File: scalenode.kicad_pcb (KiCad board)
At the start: 4 copper layers, 135.5 x 40 mm, 137 parts, among them IC1 TPS2378DDA, J1 B2B-XH-A_LF__SN_, J10 LSHM-130-01-L-RH-A-S-K-TR, J3 1-2199230-6, J4 1140084168, J5 0473460001, J6 SS-74800-144, J7 DF40HC(3.0)-100DS-0.4v, J8 DF40HC(3.0)-100DS-0.4v, M1 compute-module-4-1.5mm, Q6 BSS138-7-F, U1 TS3USB30EDGSR, U2 TPS62823DLCT, U5 TS3USB30EDGSR, U6 FT234XD-R

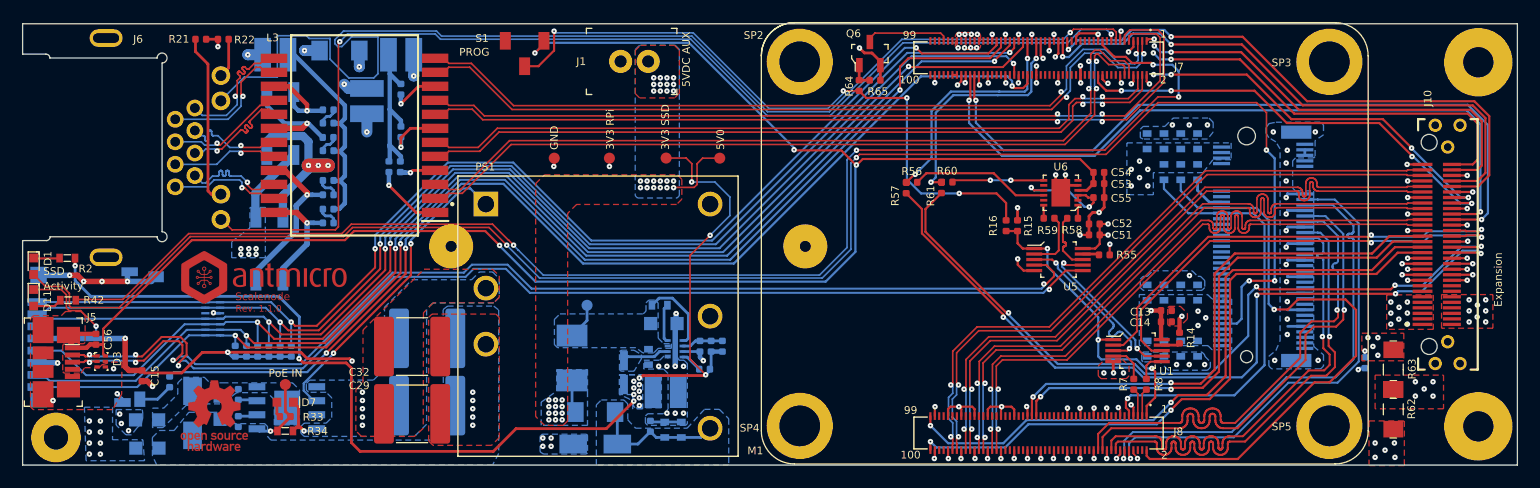
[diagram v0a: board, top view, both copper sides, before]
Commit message: Fixed and tuned differential pairs
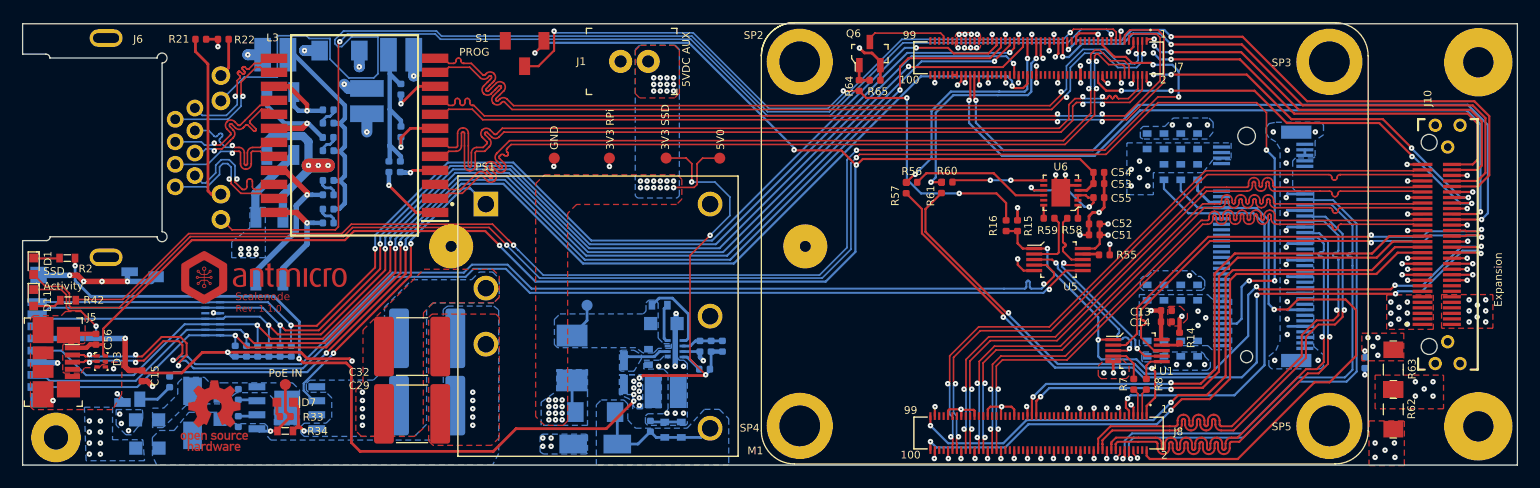
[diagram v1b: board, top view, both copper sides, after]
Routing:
- net TRD1_N: track 68.4 -> 76.9 mm
- net TRD1_P: track 69.0 -> 77.0 mm
- net TRD3_N: track 71.6 -> 77.0 mm
- net TRD3_P: track 72.1 -> 77.0 mm
- net TRD0_P: track 72.6 -> 77.0 mm
- net TRD0_N: track 73.2 -> 77.1 mm
- net /PoE/T_ETH_D1_N: track 9.76 -> 12.4 mm
- net /PoE/T_ETH_D1_P: track 9.78 -> 12.4 mm
- net /PoE/T_ETH_D0_N: track 10.1 -> 12.5 mm
- net /PoE/T_ETH_D0_P: track 10.2 -> 12.6 mm
- net TRD2_N: track 75.3 -> 77.0 mm
- net /PoE/T_ETH_D2_P: track 10.8 -> 12.5 mm
- net /PoE/T_ETH_D2_N: track 10.9 -> 12.5 mm
- net /Interfaces/CONN_USB_P: track 102.3 -> 103.5 mm
- net GND: track 155.2 -> 154.4 mm
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
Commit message: loclib
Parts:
- C26, C28, C29, C32: footprint antmicro-footprints:2220-cap -> scalenode-footprints:2220-cap
- D8: footprint antmicro-footprints:DO-214AC -> scalenode-footprints:DO-214AC
- F1: footprint antmicro-footprints:1206-res -> scalenode-footprints:1206-res
- J1: footprint antmicro-footprints:PinHeader_1x2_P2.5mm_Drill1.1mm -> scalenode-footprints:PinHeader_1x2_P2.5mm_Drill1.1mm
- PS1: footprint antmicro-footprints:PDQE30-Q48 -> scalenode-footprints:PDQE30-Q48
- R35: footprint antmicro-footprints:0402-res -> scalenode-footprints:0402-res
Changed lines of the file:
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@@
     (pad "100" smd rect (at 9.8 -1.54 180) (size 0.2 0.7) (layers "F.Cu" "F.Paste" "F.Mask")
       (net 42 "nEXTRST") (pinfunction "100") (pintype "passive"))
-    (model "${ANT3DMDL}/DF40HC_3.0_-100DS-0.4V_58.step"
+    (model "${KIPRJMOD}/lib/3d-models/DF40HC_3.0_-100DS-0.4V_58.step"
       (offset (xyz 0 0 0))
       (scale (xyz 1 1 1))
@@
     )
   )
-  (footprint "antmicro-footprints:PDQE30-Q48" (layer "F.Cu")
+  (footprint "scalenode-footprints:PDQE30-Q48" (layer "F.Cu")
     (at 127.25 83.206)
     (property "MPN" "PDQE30-Q48-S5-D")
@@
     (pad "6" thru_hole circle (at 10.16 -10.16) (size 2.25 2.25) (drill 1.5) (layers *.Cu *.Mask)
       (net 11 "GND") (pinfunction "0V") (pintype "output"))
-    (model "${ANT3DMDL}/PDQE30-Q48.step"
+    (model "${KIPRJMOD}/lib/3d-models/PDQE30-Q48.step"
       (offset (xyz 0 0 0))
       (scale (xyz 1 1 1))
@@
     )
   )
-  (footprint "antmicro-footprints:2220-cap" (layer "F.Cu")
+  (footprint "scalenode-footprints:2220-cap" (layer "F.Cu")
     (at 110.4 92.06 180)
     (descr "Capacitor SMD 2220 (5650 Metric), square (rectangular) end terminal, IPC_7351 nominal, (Body size from: http://datasheets.avx.com/AVX-HV_MLCC.pdf), generated with kicad-footprint-generator")
@@
     (pad "2" smd roundrect locked (at 2.55 0 180) (size 1.8 5.4) (layers "F.Cu" "F.Paste" "F.Mask") (roundrect_rratio 0.138889)
       (net 4 "GNDD") (pintype "passive"))
-    (model "${ANT3DMDL}/2220-cap.step"
+    (model "${KIPRJMOD}/lib/3d-models/2220-cap.step"
       (offset (xyz 0 0 0))
       (scale (xyz 1 1 1))
@@
     )
   )
-  (footprint "antmicro-footprints:PinHeader_1x2_P2.5mm_Drill1.1mm" (layer "F.Cu")
+  (footprint "scalenode-footprints:PinHeader_1x2_P2.5mm_Drill1.1mm" (layer "F.Cu")
     (at 131.8 60.115 180)
     (descr "http://www.jst-mfg.com/product/pdf/eng/eXH.pdf")
@@
     (pad "2" thru_hole circle locked (at 2.5 0 180) (size 2.1 2.1) (drill 1.1) (layers *.Cu *.Mask)
       (net 11 "GND") (pintype "passive"))
-    (model "${ANT3DMDL}/B2B-XH-A_LF__SN_.stp"
+    (model "${KIPRJMOD}/lib/3d-models/B2B-XH-A_LF__SN_.stp"
       (offset (xyz 0 0 0))
       (scale (xyz 1 1 1))
@@
     )
   )
-  (footprint "antmicro-footprints:2220-cap" (layer "F.Cu")
+  (footprint "scalenode-footprints:2220-cap" (layer "F.Cu")
     (at 110.4 85.96 180)
     (descr "Capacitor SMD 2220 (5650 Metric), square (rectangular) end terminal, IPC_7351 nominal, (Body size from: http://datasheets.avx.com/AVX-HV_MLCC.pdf), generated with kicad-footprint-generator")
@@
     (pad "2" smd roundrect locked (at 2.55 0 180) (size 1.8 5.4) (layers "F.Cu" "F.Paste" "F.Mask") (roundrect_rratio 0.138889)
       (net 4 "GNDD") (pintype "passive"))
-    (model "${ANT3DMDL}/2220-cap.step"
+    (model "${KIPRJMOD}/lib/3d-models/2220-cap.step"
       (offset (xyz 0 0 0))
       (scale (xyz 1 1 1))
@@
     )
   )
-  (footprint "antmicro-footprints:1206-res" (layer "B.Cu")
+  (footprint "scalenode-footprints:1206-res" (layer "B.Cu")
     (at 127 91.896 180)
     (descr "http://media.digikey.com/pdf/Data%20Sheets/Lite-On%20PDFs/LTST-C230KFKT_5-24-06.pdf")
@@
     (pad "2" smd rect locked (at 1.8 0 180) (size 1.5 1.8) (layers "B.Cu" "B.Paste" "B.Mask")
       (net 12 "VCC5V0") (pintype "passive"))
-    (model "${ANT3DMDL}/1206-res.step"
+    (model "${KIPRJMOD}/lib/3d-models/1206-res.step"
       (offset (xyz 0 0 0))
       (scale (xyz 1 1 1))
@@
     )
   )
-  (footprint "antmicro-footprints:DO-214AC" (layer "B.Cu")
+  (footprint "scalenode-footprints:DO-214AC" (layer "B.Cu")
     (at 127 94.796 180)
     (property "MPN" "SMAJ6.5A")
@@
     (pad "K" smd rect locked (at -2 0 180) (size 2.5 1.7) (layers "B.Cu" "B.Paste" "B.Mask")
       (net 13 "Net-(C35-Pad1)") (pintype "passive"))
-    (model "${ANT3DMDL}/DO-214AC.step"
+    (model "${KIPRJMOD}/lib/3d-models/DO-214AC.step"
       (offset (xyz 0 0 1.4))
       (scale (xyz 1 1 1))
@@
     )
   )
-  (footprint "antmicro-footprints:2220-cap" (layer "B.Cu")
+  (footprint "scalenode-footprints:2220-cap" (layer "B.Cu")
     (at 111.766 85.212 180)
     (descr "Capacitor SMD 2220 (5650 Metric), square (rectangular) end terminal, IPC_7351 nominal, (Body size from: http://datasheets.avx.com/AVX-HV_MLCC.pdf), generated with kicad-footprint-generator")
@@
     (pad "2" smd roundrect locked (at 2.55 0 180) (size 1.8 5.4) (layers "B.Cu" "B.Paste" "B.Mask") (roundrect_rratio 0.138889)
       (net 4 "GNDD") (pintype "passive"))
-    (model "${ANT3DMDL}/2220-cap.step"
+    (model "${KIPRJMOD}/lib/3d-models/2220-cap.step"
       (offset (xyz 0 0 0))
       (scale (xyz 1 1 1))
@@
     )
   )
-  (footprint "antmicro-footprints:0402-res" (layer "B.Cu")
+  (footprint "scalenode-footprints:0402-res" (layer "B.Cu")
     (at 136.911 88.0085)
     (descr "Resistor SMD 0402 (1005 Metric), square (rectangular) end terminal, IPC_7351 nominal, (Body size source: http://www.tortai-tech.com/upload/download/2011102023233369053.pdf), generated with kicad-footprint-generator")
@@
     (pad "2" smd roundrect locked (at 0.485 0) (size 0.59 0.64) (layers "B.Cu" "B.Paste" "B.Mask") (roundrect_rratio 0.25)
       (net 170 "3V3_SSD") (pintype "passive"))
-    (model "${ANT3DMDL}/0402-res.step"
+    (model "${KIPRJMOD}/lib/3d-models/0402-res.step"
       (offset (xyz 0 0 -0.01))
       (scale (xyz 1 1 1))
@@
     )
   )
-  (footprint "antmicro-footprints:2220-cap" (layer "B.Cu")
+  (footprint "scalenode-footprints:2220-cap" (layer "B.Cu")
     (at 111.766 91.312 180)
     (descr "Capacitor SMD 2220 (5650 Metric), square (rectangular) end terminal, IPC_7351 nominal, (Body size from: http://datasheets.avx.com/AVX-HV_MLCC.pdf), generated with kicad-footprint-generator")
@@
     (pad "2" smd roundrect locked (at 2.55 0 180) (size 1.8 5.4) (layers "B.Cu" "B.Paste" "B.Mask") (roundrect_rratio 0.138889)
       (net 4 "GNDD") (pintype "passive"))
-    (model "${ANT3DMDL}/2220-cap.step"
+    (model "${KIPRJMOD}/lib/3d-models/2220-cap.step"
       (offset (xyz 0 0 0))
       (scale (xyz 1 1 1))

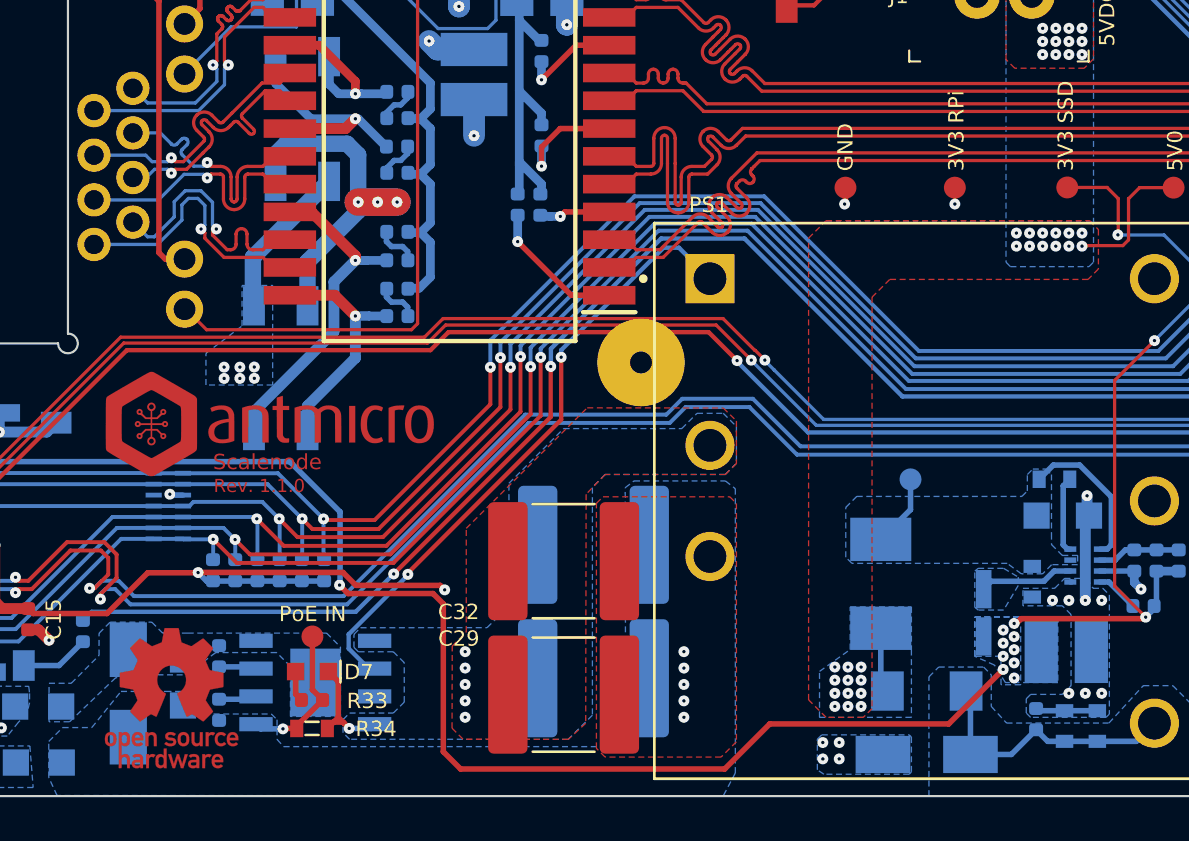
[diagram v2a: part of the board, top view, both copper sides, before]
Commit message: Corrected R33. Increased distance between L1 and L2. loclib
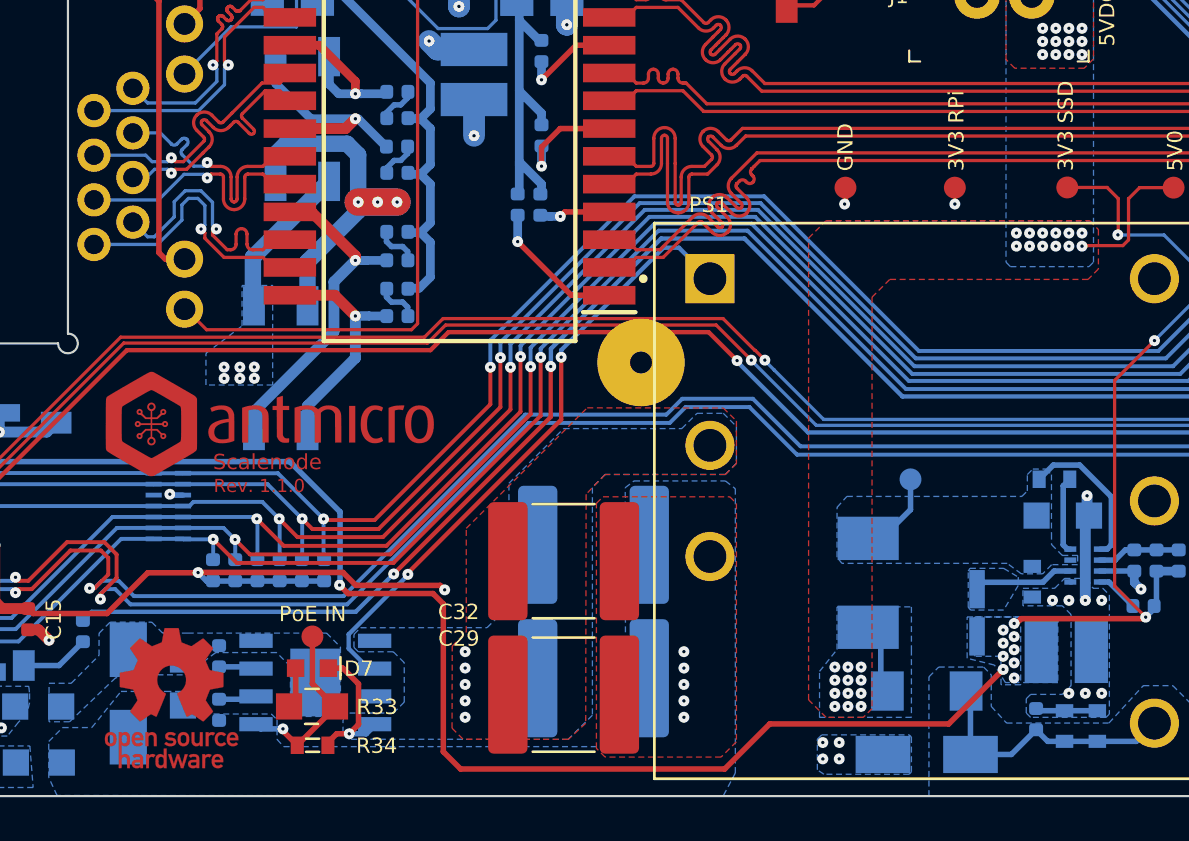
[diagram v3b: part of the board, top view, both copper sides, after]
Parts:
- R33: value R_24k9_0402 -> R_32k4_0805; footprint scalenode-footprints:0402-res -> scalenode-footprints:0805-res
- moved R34 0.77 mm to (98.9, 94.4)
- moved L1 0.58 mm to (124.3, 87.0)
- moved L2 0.30 mm to (129.3, 88.3)
- moved R33 0.29 mm to (98.9, 92.6)
- moved D7 0.16 mm to (98.9, 90.8)
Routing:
- net /PoE/VDD_POE_IN: track 6.85 -> 8.46 mm
- net GNDD: track 5.44 -> 6.74 mm
- net /PoE/T_ETH_D1_N: track 12.4 -> 11.8 mm

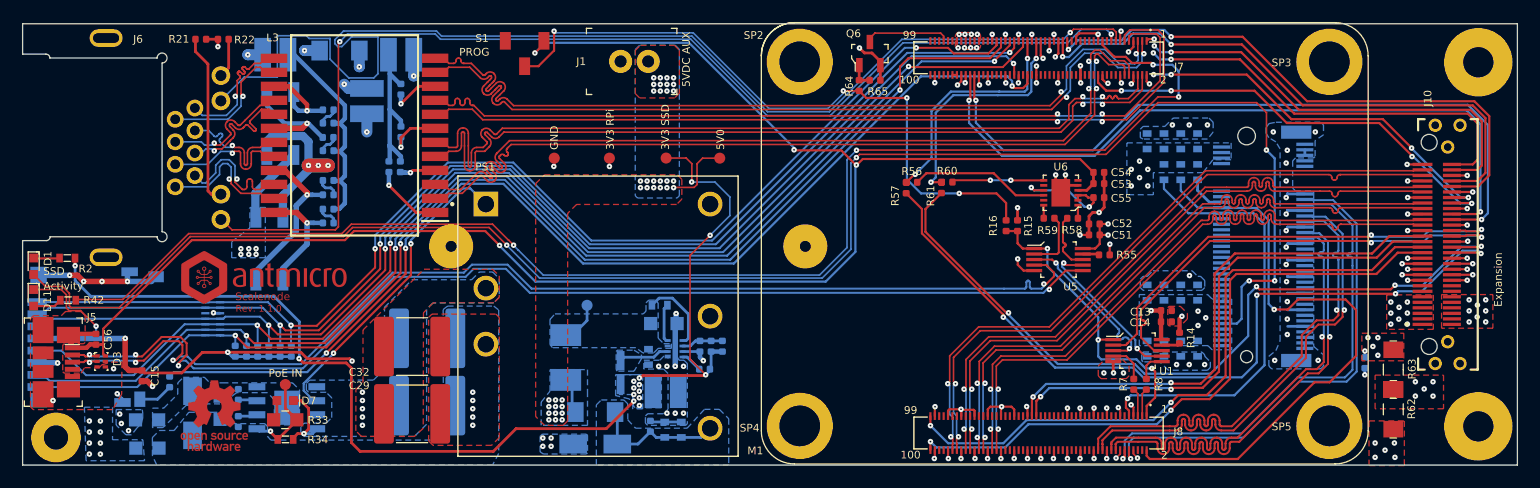
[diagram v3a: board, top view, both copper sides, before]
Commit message: Changed 3V3 converter to AP62301WU-7
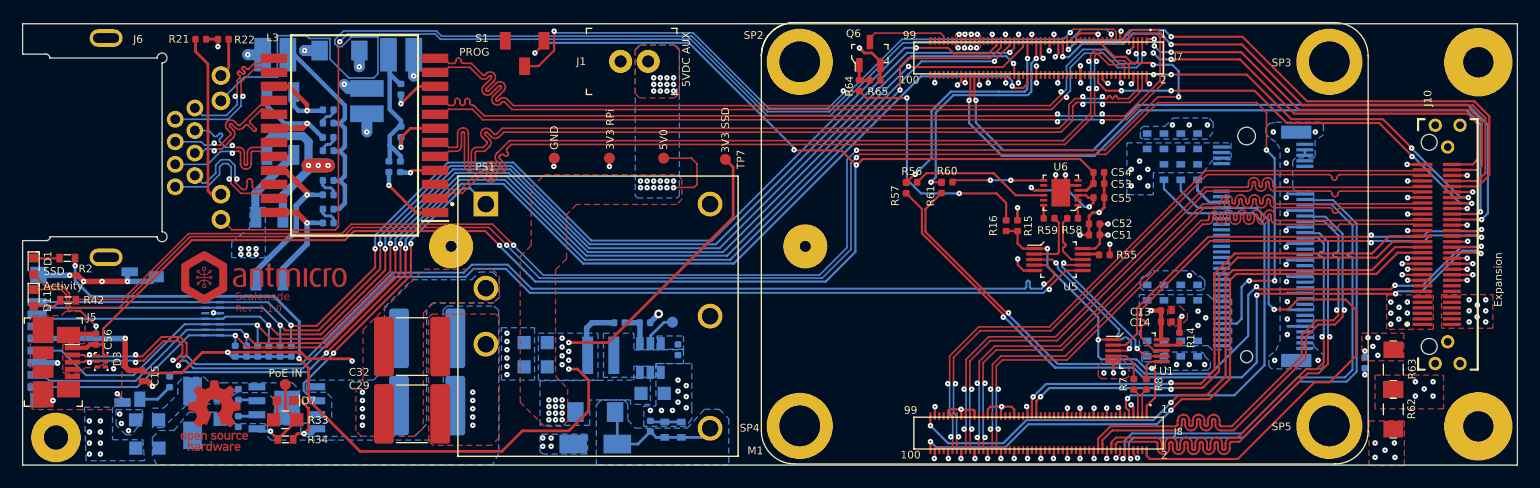
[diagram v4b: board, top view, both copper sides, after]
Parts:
- removed L2: IHLP1212AEERR47M11, scalenode-footprints:IHLP-1212AE
- removed R20: R_100k_0402, scalenode-footprints:0402-res
- removed R35: R_0R_0402, scalenode-footprints:0402-res
- removed TP1: TP_SMD1MM, scalenode-footprints:Testpoint_smd_1mm
- added TP7: TP_SMD1MM, scalenode-footprints:Testpoint_smd_1mm, F.Cu at (138.8, 69.0)
- C16: value C_22u_KEMET_A -> C_22u_0805_10V; footprint scalenode-footprints:KEMET_A -> antmicro-footprints:0805-cap
- C17: value C_4u7_0603 -> C_100n_0402; footprint scalenode-footprints:0603-cap -> antmicro-footprints:0402-cap
- C18: value C_120p_0402 -> C_22u_0805_10V; footprint scalenode-footprints:0402-res -> antmicro-footprints:0805-cap
- C19: value C_22u_1210 -> C_22u_0805_10V; footprint scalenode-footprints:1210-cap -> antmicro-footprints:0805-cap
- J7, J8: footprint scalenode-footprints:DF40HC-3.0-100DS-0.4v -> scalenode-footprints:DF40HC(3.0)-100DS-0.4v
- L1: value IHLP2020BZER4R7M01 -> XFL4020-102MEC; footprint scalenode-footprints:IHLP2020BZER4R7M01 -> antmicro-footprints:XFL4020-102MEB
- R18: value R_100k_0603 -> R_33k2_0402; footprint scalenode-footprints:0603-res -> antmicro-footprints:0402-res
- R19: value R_453k_0402 -> R_10k_0402; footprint scalenode-footprints:0402-res -> antmicro-footprints:0402-res
- TP2: moved to B.Cu
- U2: value TPS62823DLCT -> AP62301WU-7; footprint scalenode-footprints:QFN-8_2x1mm -> antmicro-footprints:TSOT23-6
- moved C18 16.9 mm to (121.6, 85.6), turned to 180 degrees
- moved TP2 14.9 mm to (134.0, 83.8), turned to 180 degrees
- moved C19 12.0 mm to (121.6, 87.8), turned to 180 degrees
- moved R19 6.37 mm to (131.5, 83.8), turned to 180 degrees
- moved C16 6.33 mm to (132.2, 90.2)
- moved TP5 5.09 mm to (133.2, 68.9)
- moved R18 3.97 mm to (129.2, 83.8), turned to 180 degrees
- moved L1 3.18 mm to (127.5, 86.8), turned to 0 degrees
- moved C17 2.75 mm to (134.5, 86.2)
- moved U2 2.39 mm to (132.0, 87.0)
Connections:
- C16 pad 1: Net-(C16-Pad1) -> VCC5V0
- C17 pad 1: Net-(C16-Pad1) -> Net-(C17-Pad1)
- C17 pad 2: GND -> Net-(C17-Pad2)
- C18 pad 2: Net-(C18-Pad2) -> GND
- L1 pad 1: VCC5V0 -> 3V3_SSD
- L1 pad 2: Net-(C16-Pad1) -> Net-(C17-Pad2)
- R18 pad 1: Net-(C16-Pad1) -> Net-(R18-Pad1)
- R18 pad 2: Net-(R18-Pad2) -> 3V3_SSD
- R19 pad 1: 3V3_SSD -> GND
- R19 pad 2: Net-(C18-Pad2) -> Net-(R18-Pad1)
- TP2 pad 1: 3V3_SSD -> Net-(TP2-Pad1)
- U2 pad 1: Net-(C16-Pad1) -> GND
- U2 pad 2: Net-(C18-Pad2) -> Net-(C17-Pad2)
- U2 pad 3: GND -> VCC5V0
- U2 pad 4: Net-(R35-Pad1) -> Net-(R18-Pad1)
- U2 pad 5: GND -> Net-(TP2-Pad1)
- U2 pad 6: Net-(L2-Pad1) -> Net-(C17-Pad1)
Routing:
- net Net-(C16-Pad1): track 10.3 -> 0.00 mm
- net GND: track 154.4 -> 144.7 mm, vias 130 -> 137
- net 3V3_SSD: track 103.4 -> 96.3 mm, vias 29 -> 25
- net Net-(L2-Pad1): track 4.61 -> 0.00 mm
- net Net-(C18-Pad2): track 3.80 -> 0.00 mm
- net Net-(R18-Pad2): track 3.53 -> 0.00 mm
- net Net-(R18-Pad1): track 0.00 -> 3.19 mm
- net Net-(TP2-Pad1): track 0.00 -> 2.97 mm
- net VCC5V0: track 9.39 -> 7.36 mm
- net Net-(R35-Pad1): track 1.97 -> 0.00 mm
- net Net-(C25-Pad2): track 15.4 -> 13.5 mm
- net HDMI0_D2_N: track 58.5 -> 57.7 mm
- net HDMI0_D1_P: track 58.6 -> 57.7 mm
- net HDMI0_D0_P: track 58.7 -> 57.8 mm
- net HDMI0_D2_P: track 58.5 -> 57.6 mm
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- added copper zone on B.Cu, net Net-(C17-Pad1)
- added copper zone on B.Cu, net Net-(C17-Pad2)
- removed copper zone on B.Cu, net Net-(C16-Pad1)
- removed copper zone on B.Cu, net Net-(L2-Pad1)
